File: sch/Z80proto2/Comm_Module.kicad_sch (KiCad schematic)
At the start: 16 parts, among them J201 Conn_01x06, J202 Conn_01x06, U201 HC138, U202 HC139, U203 TC7SH00, U204 AC74, U205 LH0082A, U206 LH0085A, U207 SN65HVD12HD

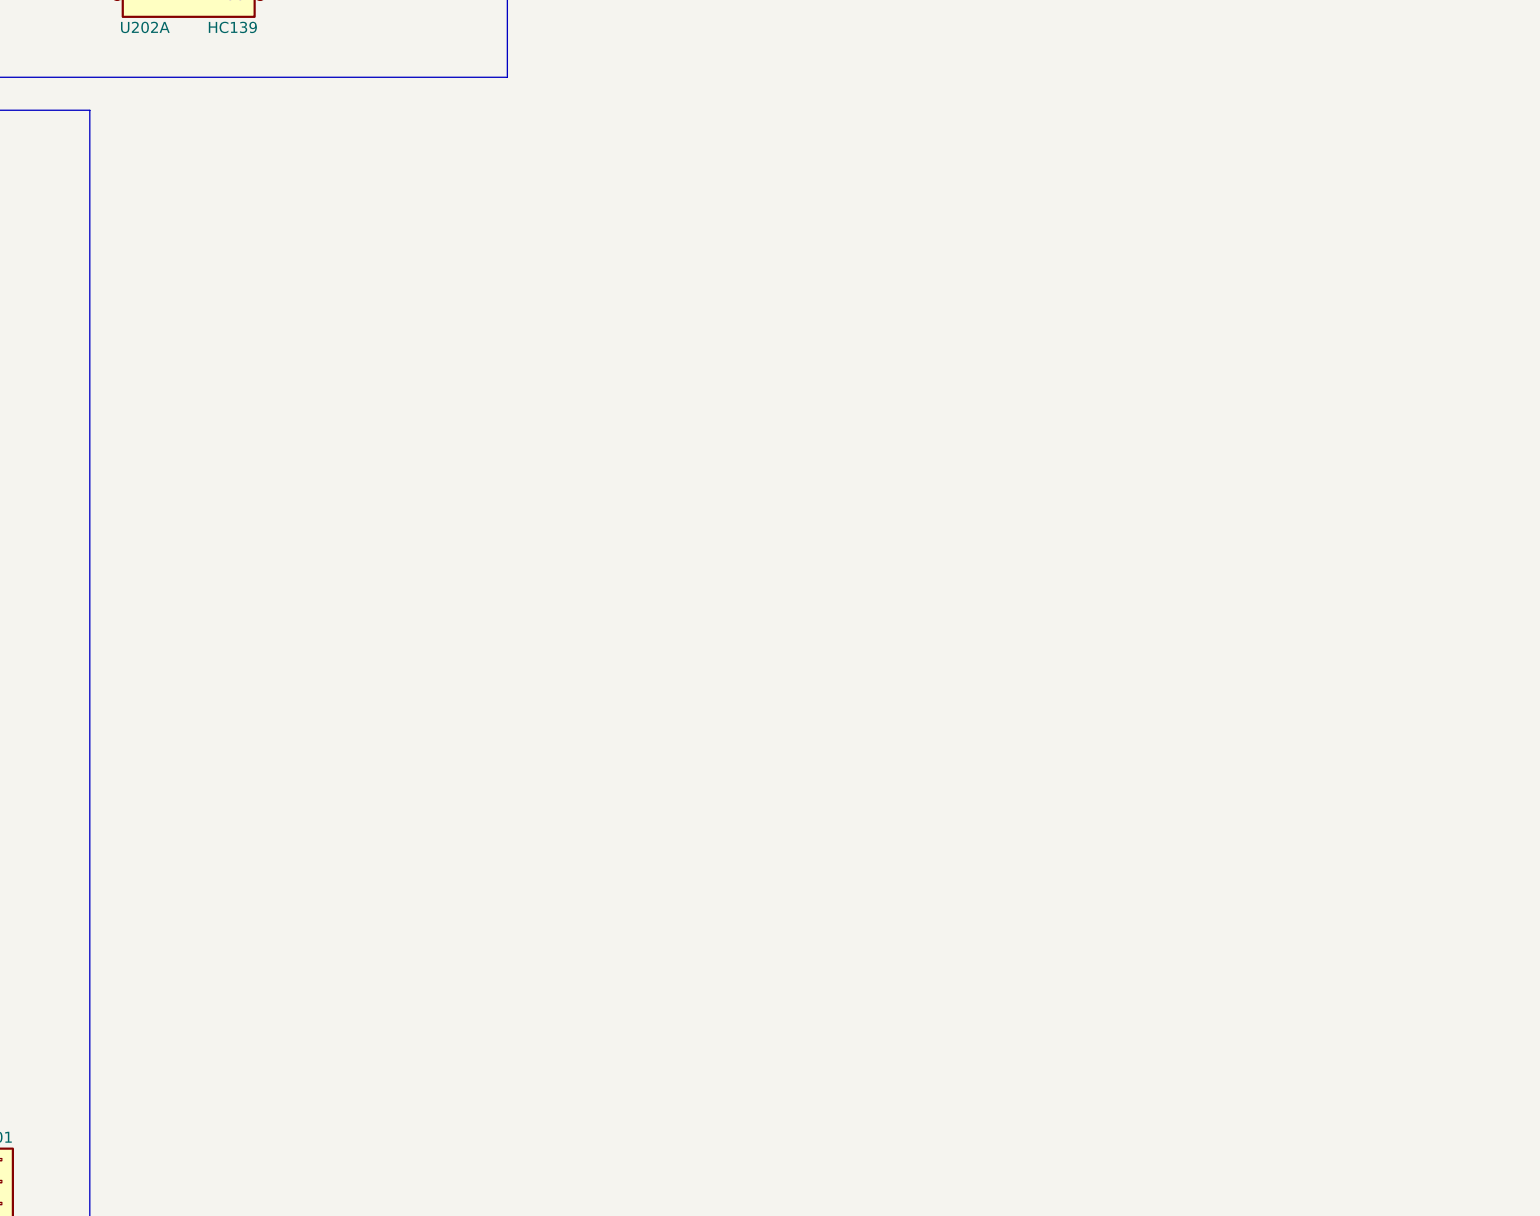
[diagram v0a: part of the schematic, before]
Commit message: Add Async. FIFO support(EXPERIMENTAL)
Add FT245R Asynchronous FIFO support(EXPERIMENTAL)
change environment MiniLoader(zcc->sdcc)
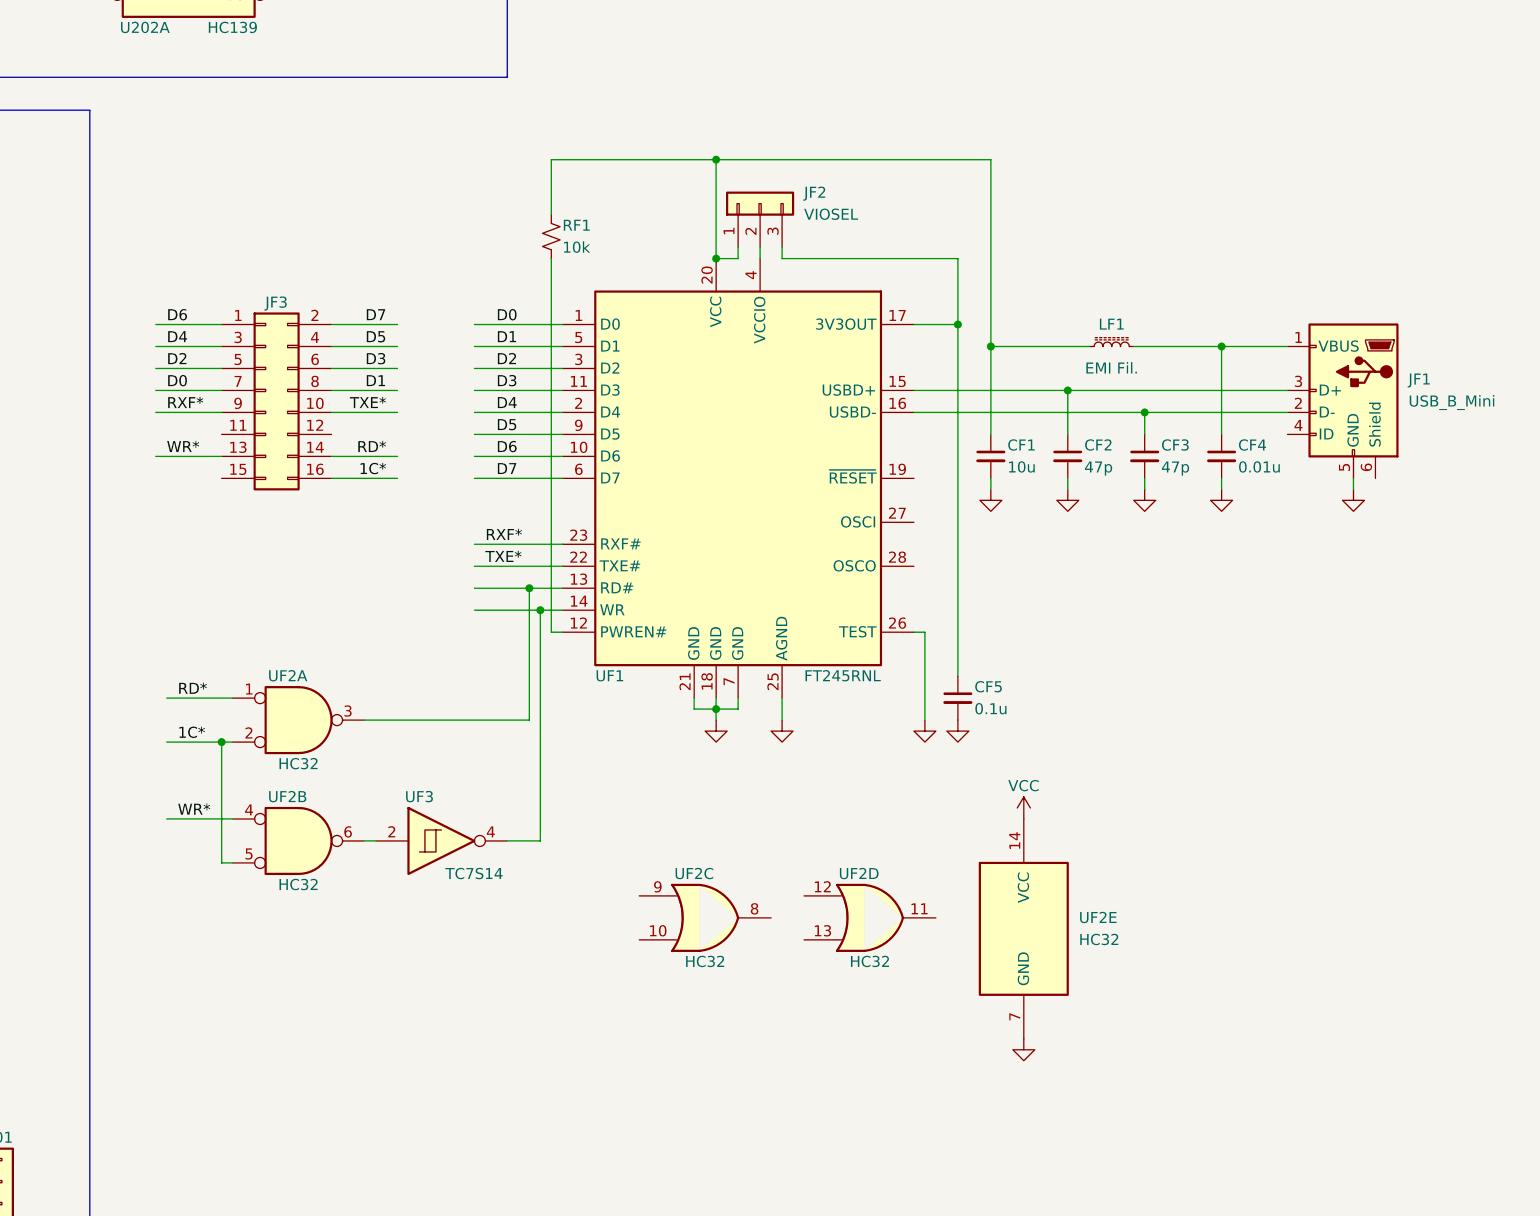
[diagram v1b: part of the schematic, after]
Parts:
- added CF1: 10u, symbol Device:C_Small
- added CF2, CF3: 47p, symbol Device:C_Small
- added CF4: 0.01u, symbol Device:C_Small
- added CF5: 0.1u, symbol Device:C_Small
- added JF1: USB_B_Mini, symbol Connector:USB_B_Mini
- added JF2: VIOSEL, symbol Connector_Generic:Conn_01x03
- added JF3: Conn_02x08_Odd_Even, symbol Connector_Generic:Conn_02x08_Odd_Even
- added LF1: EMI Fil., symbol Device:L_Ferrite_Small
- added RF1: 10k, symbol Device:R_Small_US
- added UF1: FT245RNL, symbol FT245RNL:FT245RNL
- added UF2: HC32, symbol 74xx:74LS32
- added UF3: TC7S14, symbol Toshiba_Sp:TC7S14
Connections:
- net 1C*: now also JF3.16 (Pin_16), UF2.2, UF2.5
- net D0: now also JF3.7 (Pin_7), UF1.1 (D0)
- net D1: now also JF3.8 (Pin_8), UF1.5 (D1)
- net D2: now also JF3.5 (Pin_5), UF1.3 (D2)
- net D3: now also JF3.6 (Pin_6), UF1.11 (D3)
- net D4: now also JF3.3 (Pin_3), UF1.2 (D4)
- net D5: now also JF3.4 (Pin_4), UF1.9 (D5)
- net D6: now also JF3.1 (Pin_1), UF1.10 (D6)
- net D7: now also JF3.2 (Pin_2), UF1.6 (D7)
- net GND: now also CF1.2, CF2.2, CF3.2, CF4.2, CF5.2, JF1.5 (GND), UF1.18 (GND), UF1.21 (GND), UF1.25 (AGND), UF1.26 (TEST), UF1.7 (GND), UF2.7 (GND)
- net RD*: now also JF3.14 (Pin_14), UF2.1
- net VCC: now also UF2.14 (VCC)
- new net: UF2.6, UF3.2
- new net: UF1.14 (WR), UF3.4
- new net: CF2.1, JF1.3 (D+), UF1.15 (USBD+)
- new net: CF4.1, JF1.1 (VBUS), LF1.2
- new net: CF3.1, JF1.2 (D-), UF1.16 (USBD-)
- new net: RF1.2, UF1.12 (PWREN#)
- new net: UF1.13 (RD#), UF2.3
- new net: CF5.1, JF2.3 (Pin_3), UF1.17 (3V3OUT)
- new net: CF1.1, JF2.1 (Pin_1), LF1.1, RF1.1, UF1.20 (VCC)
- new net: JF2.2 (Pin_2), UF1.4 (VCCIO)
- new net RXF*: JF3.9 (Pin_9), UF1.23 (RXF#)
- new net TXE*: JF3.10 (Pin_10), UF1.22 (TXE#)
- new net WR*: JF3.13 (Pin_13), UF2.4

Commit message: EXPERIMENTAL : add reset* for FT245R
add reset line ...
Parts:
- added SW? (x2): SW_DPDT_x2, symbol Switch:SW_DPDT_x2
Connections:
- net RD*: now also SW?.1 (A)
- net RES*: now also JF3.15 (Pin_15), UF1.19 (~{RESET})
- net WR*: now also SW?.4 (A)
- net at UF1.14 (WR): now also SW?.5 (B); no longer UF3.4
- net at UF2.3: now also SW?.3 (C); no longer UF1.13 (RD#)
- new net: SW?.6 (C), UF3.4
- new net: SW?.2 (B), UF1.13 (RD#)
